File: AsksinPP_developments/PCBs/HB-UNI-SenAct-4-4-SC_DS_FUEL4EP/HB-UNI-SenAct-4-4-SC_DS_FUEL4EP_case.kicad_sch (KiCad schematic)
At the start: 27 parts, among them J1 5V supply, J3 4x Relais, J4 5x LEDs, J5 4x Push Buttons, J6 Accumulator, SW1 Heating, SW2 Monitor, SW3 Hifiberry, SW4 AC supply

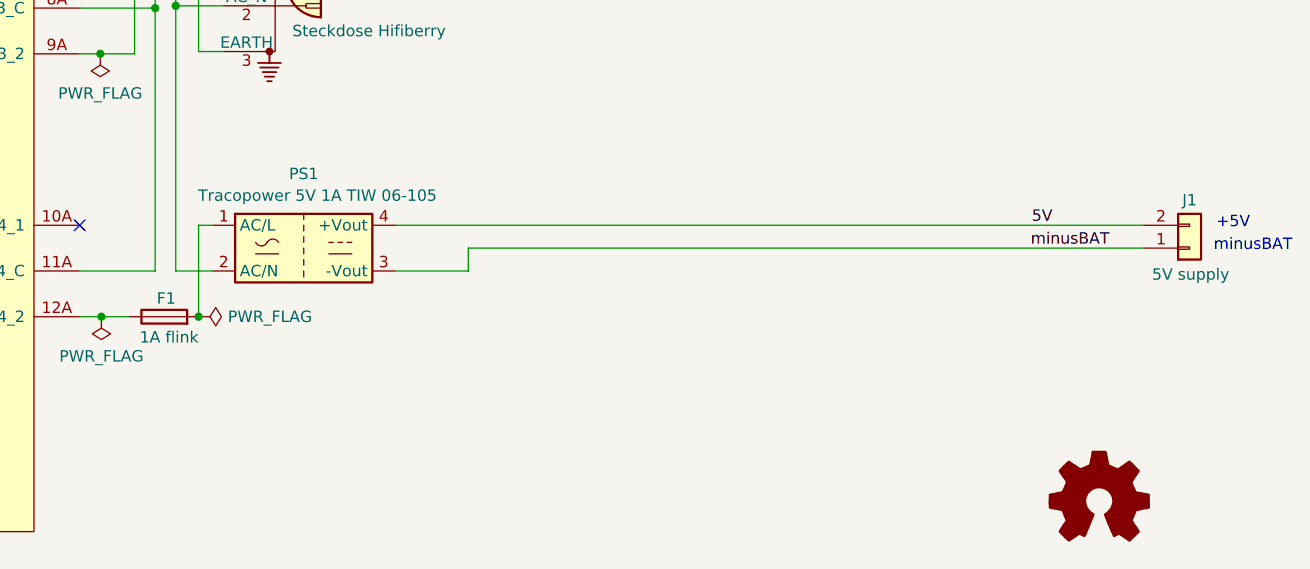
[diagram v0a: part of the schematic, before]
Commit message: HB-UNI-SenAct-4-4-SC_DS_FUEL4EP: some minor updates to prevent a slightly glowing blue LED in darkness
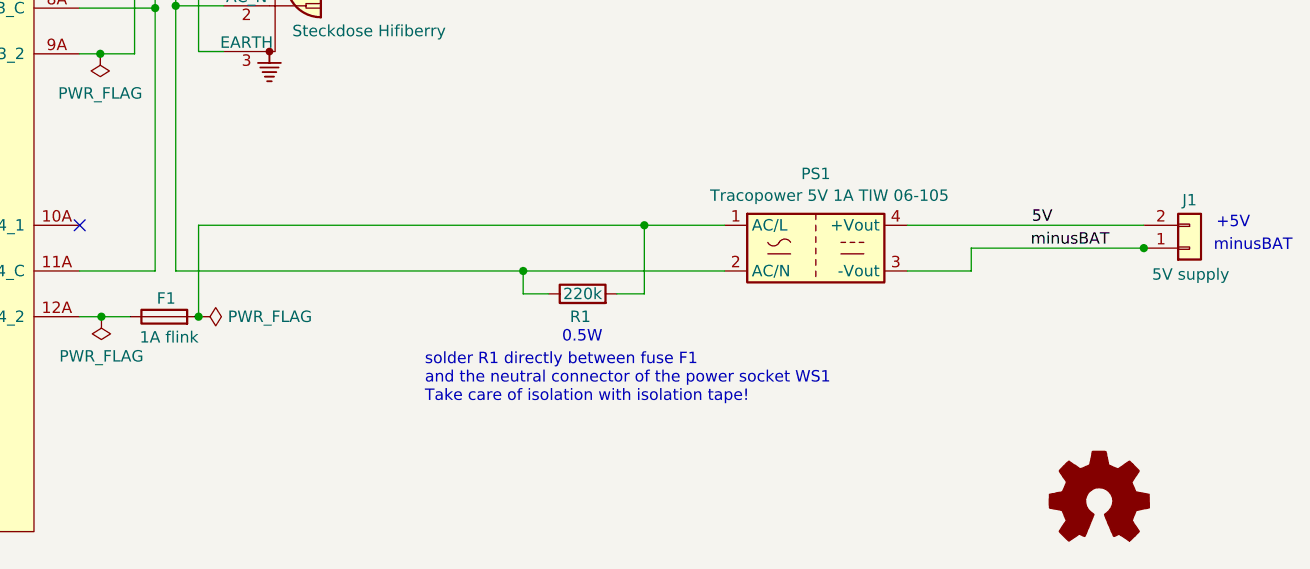
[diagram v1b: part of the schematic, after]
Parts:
- added R1: 220k, symbol Device:R
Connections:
- net at F1.2, PS1.1 (AC/L): now also R1.2
- net at PS1.2 (AC/N), WP1.2 (AC_N), WP2.2 (AC_N)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: now also R1.1
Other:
- note added: "0.5W"
- note added: "solder R1 directly between fuse F1 and the neutral connector of the power socket WS1 Take care of isolation with isolation tape!"
- moved on the sheet: PS1
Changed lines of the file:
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@@
   (title_block
     (title "HB-UNI-SenAct-4-4-SC_DS_FUEL4EP")
-    (date "2021-10-01")
-    (rev "1.0")
+    (date "2023-07-19")
+    (rev "1.1")
     (company "FUEL4EP")
     (comment 1 "3x Schaltaktor AsksinPP für Netzfreischalter Gehäusebauteile")
@@
   (junction (at 80.01 183.515) (diameter 0) (color 0 0 0 0)
   )
+  (junction (at 266.827 146.304) (diameter 0) (color 0 0 0 0)
+  )
   (junction (at 54.61 87.63) (diameter 0) (color 0 0 0 0)
   )
@@
   )
   (junction (at 159.258 119.38) (diameter 0) (color 0 0 0 0)
+  )
+  (junction (at 211.328 143.764) (diameter 0) (color 0 0 0 0)
+  )
+  (junction (at 197.866 148.844) (diameter 0) (color 0 0 0 0)
   )
   (junction (at 54.61 74.93) (diameter 0) (color 0 0 0 0)
@@
     (stroke (width 0) (type default) (color 0 0 0 0))
   )
+  (wire (pts (xy 211.328 143.764) (xy 220.218 143.764))
+    (stroke (width 0) (type default) (color 0 0 0 0))
+  )
+  (wire (pts (xy 211.328 151.384) (xy 211.328 143.764))
+    (stroke (width 0) (type default) (color 0 0 0 0))
+  )
   (wire (pts (xy 80.01 168.275) (xy 80.01 173.355))
     (stroke (width 0) (type default) (color 0 0 0 0))
   )
+  (wire (pts (xy 247.65 146.304) (xy 266.827 146.304))
+    (stroke (width 0) (type default) (color 0 0 0 0))
+  )
   (wire (pts (xy 62.23 183.515) (xy 46.99 183.515))
     (stroke (width 0) (type default) (color 0 0 0 0))
@@
     (stroke (width 0) (type default) (color 0 0 0 0))
   )
+  (wire (pts (xy 266.827 146.304) (xy 266.954 146.304))
+    (stroke (width 0) (type default) (color 0 0 0 0))
+  )
   (wire (pts (xy 154.686 124.714) (xy 154.686 114.3))
     (stroke (width 0) (type default) (color 0 0 0 0))
@@
     (stroke (width 0) (type default) (color 0 0 0 0))
   )
+  (wire (pts (xy 197.866 151.384) (xy 197.866 148.844))
+    (stroke (width 0) (type default) (color 0 0 0 0))
+  )
+  (wire (pts (xy 208.28 151.384) (xy 211.328 151.384))
+    (stroke (width 0) (type default) (color 0 0 0 0))
+  )
   (wire (pts (xy 50.165 188.595) (xy 50.165 186.055))
     (stroke (width 0) (type default) (color 0 0 0 0))
@@
     (stroke (width 0) (type default) (color 0 0 0 0))
   )
-  (wire (pts (xy 159.258 148.844) (xy 163.322 148.844))
+  (wire (pts (xy 159.258 148.844) (xy 197.866 148.844))
     (stroke (width 0) (type default) (color 0 0 0 0))
   )
@@
     (stroke (width 0) (type default) (color 0 0 0 0))
   )
-  (wire (pts (xy 191.77 146.304) (xy 191.77 148.844))
-    (stroke (width 0) (type default) (color 0 0 0 0))
-  )
   (wire (pts (xy 47.625 77.47) (xy 102.87 77.47))
     (stroke (width 0) (type default) (color 0 0 0 0))
@@
     (stroke (width 0) (type default) (color 0 0 0 0))
   )
-  (wire (pts (xy 191.77 146.304) (xy 266.827 146.304))
-    (stroke (width 0) (type default) (color 0 0 0 0))
-  )
   (wire (pts (xy 80.01 163.195) (xy 80.01 168.275))
     (stroke (width 0) (type default) (color 0 0 0 0))
@@
     (stroke (width 0) (type default) (color 0 0 0 0))
   )
-  (wire (pts (xy 191.77 148.844) (xy 183.642 148.844))
-    (stroke (width 0) (type default) (color 0 0 0 0))
-  )
-  (wire (pts (xy 161.798 143.764) (xy 163.322 143.764))
+  (wire (pts (xy 161.798 143.764) (xy 211.328 143.764))
     (stroke (width 0) (type default) (color 0 0 0 0))
   )
@@
     (stroke (width 0) (type default) (color 0 0 0 0))
   )
+  (wire (pts (xy 247.65 148.844) (xy 240.538 148.844))
+    (stroke (width 0) (type default) (color 0 0 0 0))
+  )
   (wire (pts (xy 118.11 186.055) (xy 118.11 182.88))
     (stroke (width 0) (type default) (color 0 0 0 0))
@@
     (stroke (width 0) (type default) (color 0 0 0 0))
   )
+  (wire (pts (xy 197.866 148.844) (xy 220.218 148.844))
+    (stroke (width 0) (type default) (color 0 0 0 0))
+  )
   (wire (pts (xy 154.686 53.34) (xy 154.686 63.754))
     (stroke (width 0) (type default) (color 0 0 0 0))
@@
     (stroke (width 0) (type default) (color 0 0 0 0))
   )
+  (wire (pts (xy 200.66 151.384) (xy 197.866 151.384))
+    (stroke (width 0) (type default) (color 0 0 0 0))
+  )
   (wire (pts (xy 154.178 153.924) (xy 151.003 153.924))
     (stroke (width 0) (type default) (color 0 0 0 0))
@@
     (stroke (width 0) (type default) (color 0 0 0 0))
   )
-  (wire (pts (xy 183.642 143.764) (xy 266.827 143.764))
+  (wire (pts (xy 240.538 143.764) (xy 266.827 143.764))
     (stroke (width 0) (type default) (color 0 0 0 0))
   )
@@
   )
   (wire (pts (xy 81.28 136.906) (xy 81.28 141.351))
+    (stroke (width 0) (type default) (color 0 0 0 0))
+  )
+  (wire (pts (xy 247.65 146.304) (xy 247.65 148.844))
     (stroke (width 0) (type default) (color 0 0 0 0))
   )
@@
     (effects (font (size 1.27 1.27)) (justify left bottom))
   )
+  (text "solder R1 directly between fuse F1\nand the neutral connector of the power socket WS1\nTake care of isolation with isolation tape!"
+    (at 186.944 163.576 0)
+    (effects (font (size 1.27 1.27)) (justify left bottom))
+  )
   (text "Hifiberry\n" (at 29.21 129.286 0)
+    (effects (font (size 1.27 1.27)) (justify left bottom))
+  )
+  (text "0.5W" (at 202.184 156.972 0)
     (effects (font (size 1.27 1.27)) (justify left bottom))
   )
@@
     (pin "3")
   )
-  (symbol (lib_id "Converter_ACDC:HLK-PM01") (at 173.482 146.304 0) (unit 1)
-    (in_bom yes) (on_board yes)
-    (property "Reference" "PS1" (id 0) (at 173.482 138.049 0))
-    (property "Value" "Tracopower 5V 1A TIW 06-105" (id 1) (at 175.006 140.462 0))
-    (property "Footprint" "Converter_ACDC:Converter_ACDC_HiLink_HLK-PMxx" (id 2) (at 173.482 153.924 0)
-      (effects (font (size 1.27 1.27)) hide)
-    )
-    (property "Datasheet" "http://www.hlktech.net/product_detail.php?ProId=54" (id 3) (at 183.642 155.194 0)
+  (symbol (lib_id "Converter_ACDC:HLK-PM01") (at 230.378 146.304 0) (unit 1)
+    (in_bom yes) (on_board yes)
+    (property "Reference" "PS1" (id 0) (at 230.378 138.049 0))
+    (property "Value" "Tracopower 5V 1A TIW 06-105" (id 1) (at 231.902 140.462 0))
+    (property "Footprint" "Converter_ACDC:Converter_ACDC_HiLink_HLK-PMxx" (id 2) (at 230.378 153.924 0)
+      (effects (font (size 1.27 1.27)) hide)
+    )
+    (property "Datasheet" "http://www.hlktech.net/product_detail.php?ProId=54" (id 3) (at 240.538 155.194 0)
       (effects (font (size 1.27 1.27)) hide)
     )
@@
     (pin "1")
   )
+  (symbol (lib_id "Device:R") (at 204.47 151.384 90) (unit 1)
+    (in_bom yes) (on_board yes)
+    (property "Reference" "R1" (id 0) (at 204.216 153.924 90))
+    (property "Value" "220k" (id 1) (at 204.47 151.384 90))
+    (property "Footprint" "" (id 2) (at 204.47 153.162 90)
+      (effects (font (size 1.27 1.27)) hide)
+    )
+    (property "Datasheet" "~" (id 3) (at 204.47 151.384 0)
+      (effects (font (size 1.27 1.27)) hide)
+    )
+    (pin "1")
+    (pin "2")
+  )
   (sheet_instances
     (path "/" (page "1"))
@@
       (reference "PS1") (unit 1) (value "Tracopower 5V 1A TIW 06-105") (footprint "Converter_ACDC:Converter_ACDC_HiLink_HLK-PMxx")
     )
+    (path "/e8a2e593-c800-4495-a3ba-c9787eb74f1e"
+      (reference "R1") (unit 1) (value "220k") (footprint "")
+    )
     (path "/00000000-0000-0000-0000-00006197bac3"

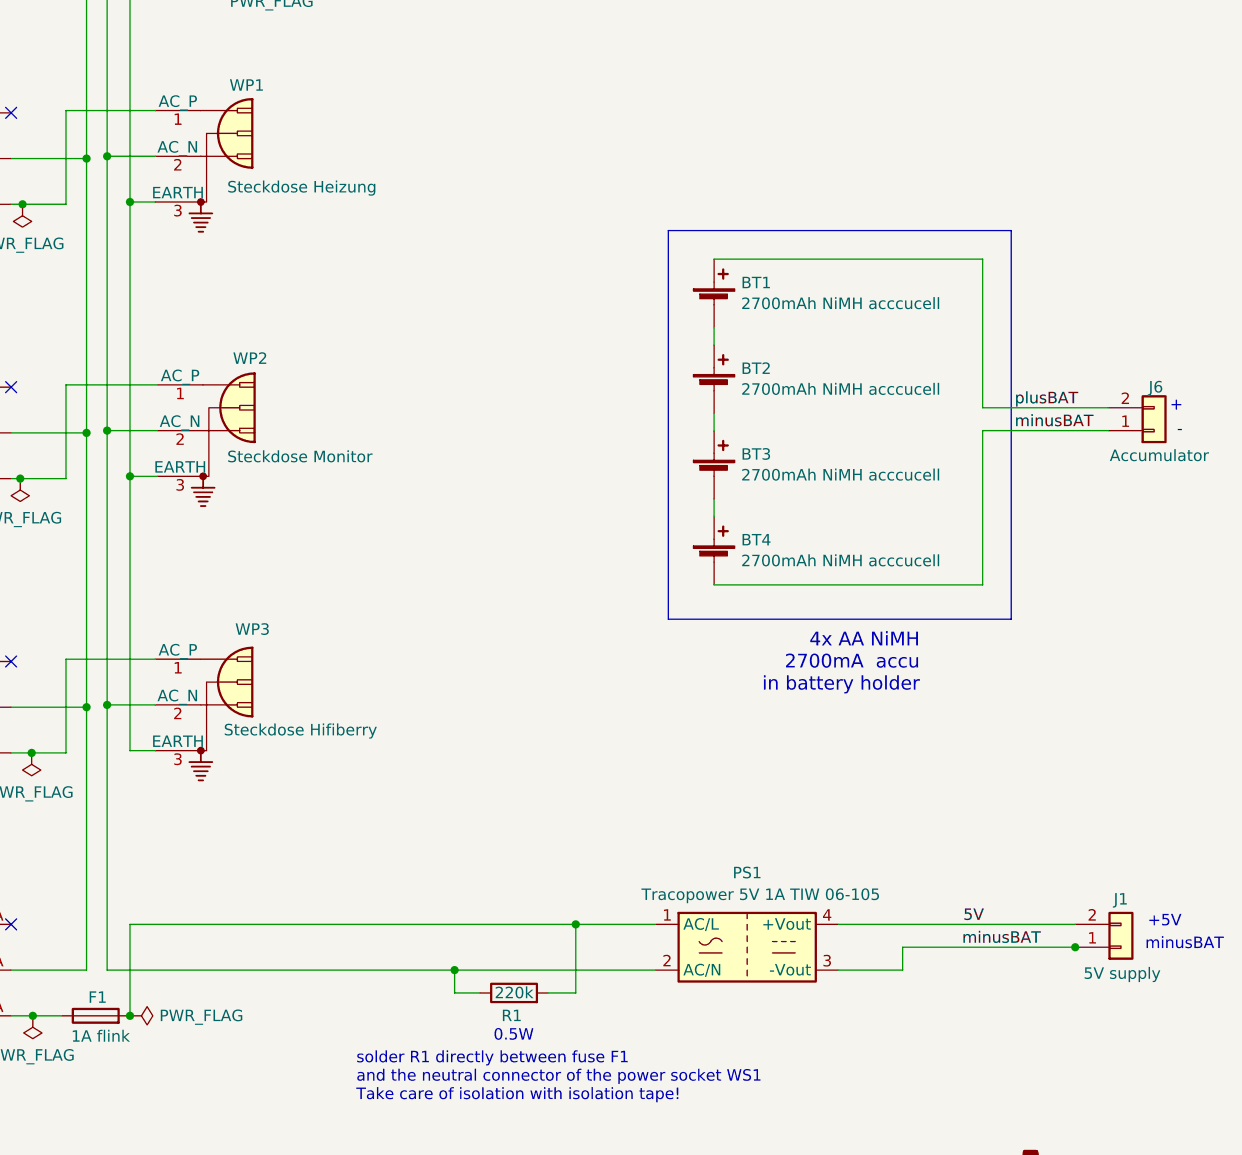
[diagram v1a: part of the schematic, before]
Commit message: HB-UNI-SenAct-4-4-SC_DS_FUEL4EP: add supressor capacitor; documentation updates
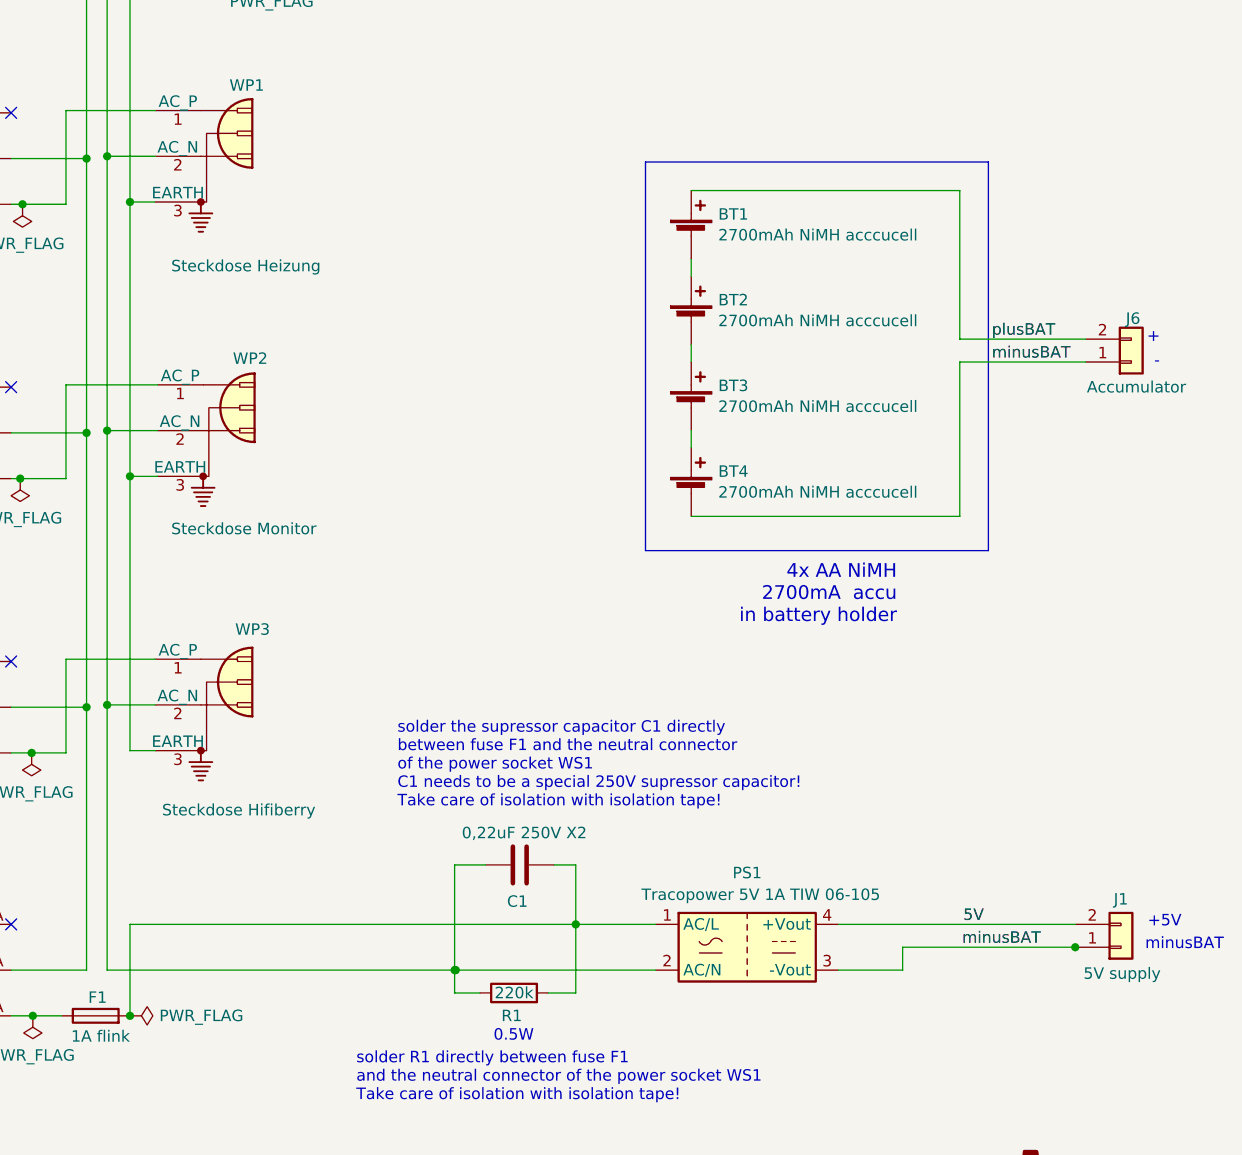
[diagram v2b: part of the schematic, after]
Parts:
- added C1: 0,22uF 250V X2, symbol Device:C
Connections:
- net at F1.2, PS1.1 (AC/L), R1.2: now also C1.2
- net at PS1.2 (AC/N), R1.1, WP1.2 (AC_N)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: now also C1.1
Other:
- note added: "solder the supressor capacitor C1 directly between fuse F1 and the neutral connector of the power socket WS1 C1 needs to be a special 250V supressor capacitor! Take care of isolation with isolation tape!"
- moved on the sheet: BT1, BT2, BT3, BT4, J6
